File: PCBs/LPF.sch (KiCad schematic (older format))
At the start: 9 parts, among them J2 ANT

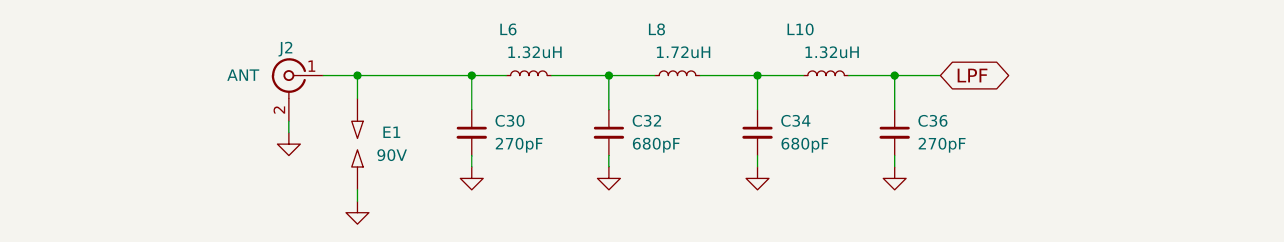
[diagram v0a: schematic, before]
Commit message: ADX988 CAT: add FE, FI commands
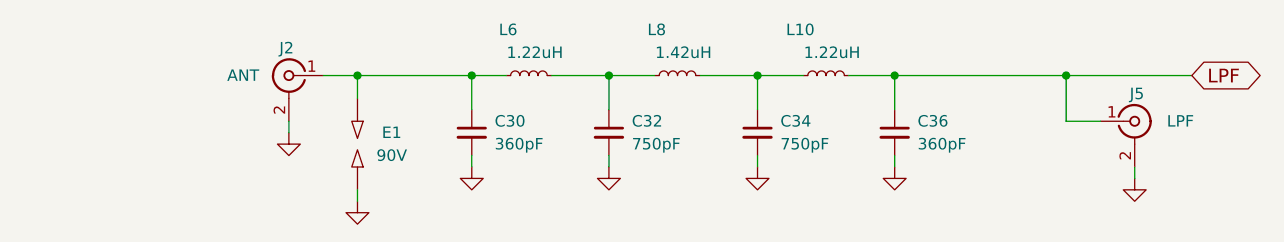
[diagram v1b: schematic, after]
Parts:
- added J5: LPF, LCSDR:U.FL_Molex_MCRF_73412-0110_Vertical, symbol Conn_Coaxial
- C30, C36: value 270pF -> 360pF; footprint Capacitors_THT:C_Disc_D4.7mm_W2.5mm_P5.00mm -> LCSDR:C_1206_0603
- C32, C34: value 680pF -> 750pF; footprint Capacitors_THT:C_Disc_D4.7mm_W2.5mm_P5.00mm -> LCSDR:C_1206_0603
- L10, L6: value 1.32uH -> 1.22uH; footprint Choke_Axial_ThroughHole:Choke_Horizontal_RM20mm -> Choke_Toroid_ThroughHole:Choke_Toroid_6,5x13mm_Vertical
- L8: value 1.72uH -> 1.42uH; footprint Choke_Axial_ThroughHole:Choke_Horizontal_RM20mm -> Choke_Toroid_ThroughHole:Choke_Toroid_6,5x13mm_Vertical
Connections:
- net GND: now also J5.2 (Ext)
- net LPF: now also J5.1 (In)
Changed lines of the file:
@@
 $Descr A4 11693 8268
 encoding utf-8
-Sheet 7 9
+Sheet 7 8
 Title ""
 Date ""
@@
 P 5200 2400
 F 0 "L6" V 5400 2450 50  0000 L CNN
-F 1 "1.32uH" V 5300 2250 50  0000 L CNN
-F 2 "Choke_Axial_ThroughHole:Choke_Horizontal_RM20mm" H 5200 2400 50  0001 C CNN
+F 1 "1.22uH" V 5300 2250 50  0000 L CNN
+F 2 "Choke_Toroid_ThroughHole:Choke_Toroid_6,5x13mm_Vertical" H 5200 2400 50  0001 C CNN
 F 3 "" H 5200 2400 50  0001 C CNN
 	1    5200 2400
@@
 P 5550 2650
 F 0 "C32" H 5650 2700 50  0000 L CNN
-F 1 "680pF" H 5650 2600 50  0000 L CNN
-F 2 "Capacitors_THT:C_Disc_D4.7mm_W2.5mm_P5.00mm" H 5550 2650 50  0001 C CNN
+F 1 "750pF" H 5650 2600 50  0000 L CNN
+F 2 "LCSDR:C_1206_0603" H 5550 2650 50  0001 C CNN
 F 3 "" H 5550 2650 50  0001 C CNN
 	1    5550 2650
@@
 P 4950 2650
 F 0 "C30" H 5050 2700 50  0000 L CNN
-F 1 "270pF" H 5050 2600 50  0000 L CNN
-F 2 "Capacitors_THT:C_Disc_D4.7mm_W2.5mm_P5.00mm" H 4950 2650 50  0001 C CNN
+F 1 "360pF" H 5050 2600 50  0000 L CNN
+F 2 "LCSDR:C_1206_0603" H 4950 2650 50  0001 C CNN
 F 3 "" H 4950 2650 50  0001 C CNN
 	1    4950 2650
@@
 P 5850 2400
 F 0 "L8" V 6050 2450 50  0000 L CNN
-F 1 "1.72uH" V 5950 2250 50  0000 L CNN
-F 2 "Choke_Axial_ThroughHole:Choke_Horizontal_RM20mm" H 5850 2400 50  0001 C CNN
+F 1 "1.42uH" V 5950 2250 50  0000 L CNN
+F 2 "Choke_Toroid_ThroughHole:Choke_Toroid_6,5x13mm_Vertical" H 5850 2400 50  0001 C CNN
 F 3 "" H 5850 2400 50  0001 C CNN
 	1    5850 2400
@@
 P 6500 2400
 F 0 "L10" V 6700 2450 50  0000 L CNN
-F 1 "1.32uH" V 6600 2250 50  0000 L CNN
-F 2 "Choke_Axial_ThroughHole:Choke_Horizontal_RM20mm" H 6500 2400 50  0001 C CNN
+F 1 "1.22uH" V 6600 2250 50  0000 L CNN
+F 2 "Choke_Toroid_ThroughHole:Choke_Toroid_6,5x13mm_Vertical" H 6500 2400 50  0001 C CNN
 F 3 "" H 6500 2400 50  0001 C CNN
 	1    6500 2400
@@
 $EndComp
 $Comp
-L GND #PWR084
+L GND #PWR92
 U 1 1 630B845A
 P 4950 2800
-F 0 "#PWR084" H 4950 2550 50  0001 C CNN
+F 0 "#PWR92" H 4950 2550 50  0001 C CNN
 F 1 "GND" H 4950 2650 50  0001 C CNN
 F 2 "" H 4950 2800 50  0001 C CNN
@@
 	4950 2800 4950 2750
 $Comp
-L GND #PWR085
+L GND #PWR93
 U 1 1 630B84B3
 P 5550 2800
-F 0 "#PWR085" H 5550 2550 50  0001 C CNN
+F 0 "#PWR93" H 5550 2550 50  0001 C CNN
 F 1 "GND" H 5550 2650 50  0001 C CNN
 F 2 "" H 5550 2800 50  0001 C CNN
@@
 	5550 2800 5550 2750
 $Comp
-L GND #PWR086
+L GND #PWR94
 U 1 1 630B84EC
 P 6200 2800
-F 0 "#PWR086" H 6200 2550 50  0001 C CNN
+F 0 "#PWR94" H 6200 2550 50  0001 C CNN
 F 1 "GND" H 6200 2650 50  0001 C CNN
 F 2 "" H 6200 2800 50  0001 C CNN
@@
 P 6200 2650
 F 0 "C34" H 6300 2700 50  0000 L CNN
-F 1 "680pF" H 6300 2600 50  0000 L CNN
-F 2 "Capacitors_THT:C_Disc_D4.7mm_W2.5mm_P5.00mm" H 6200 2650 50  0001 C CNN
+F 1 "750pF" H 6300 2600 50  0000 L CNN
+F 2 "LCSDR:C_1206_0603" H 6200 2650 50  0001 C CNN
 F 3 "" H 6200 2650 50  0001 C CNN
 	1    6200 2650
@@
 	6200 2750 6200 2800
 Wire Wire Line
-	6600 2400 7000 2400
+	6600 2400 8100 2400
 Wire Wire Line
 	6800 2400 6800 2550
 $Comp
-L GND #PWR087
+L GND #PWR95
 U 1 1 630B859B
 P 6800 2800
-F 0 "#PWR087" H 6800 2550 50  0001 C CNN
+F 0 "#PWR95" H 6800 2550 50  0001 C CNN
 F 1 "GND" H 6800 2650 50  0001 C CNN
 F 2 "" H 6800 2800 50  0001 C CNN
@@
 P 6800 2650
 F 0 "C36" H 6900 2700 50  0000 L CNN
-F 1 "270pF" H 6900 2600 50  0000 L CNN
-F 2 "Capacitors_THT:C_Disc_D4.7mm_W2.5mm_P5.00mm" H 6800 2650 50  0001 C CNN
+F 1 "360pF" H 6900 2600 50  0000 L CNN
+F 2 "LCSDR:C_1206_0603" H 6800 2650 50  0001 C CNN
 F 3 "" H 6800 2650 50  0001 C CNN
 	1    6800 2650
@@
 Connection ~ 4450 2400
 $Comp
-L GND #PWR088
+L GND #PWR91
 U 1 1 630B8EE3
 P 4450 2950
-F 0 "#PWR088" H 4450 2700 50  0001 C CNN
+F 0 "#PWR91" H 4450 2700 50  0001 C CNN
 F 1 "GND" H 4450 2800 50  0001 C CNN
 F 2 "" H 4450 2950 50  0001 C CNN
@@
 	4450 2950 4450 2900
 $Comp
-L GND #PWR089
+L GND #PWR90
 U 1 1 630B8F7F
 P 4150 2650
-F 0 "#PWR089" H 4150 2400 50  0001 C CNN
+F 0 "#PWR90" H 4150 2400 50  0001 C CNN
 F 1 "GND" H 4150 2500 50  0001 C CNN
 F 2 "" H 4150 2650 50  0001 C CNN
@@
 	4150 2650 4150 2600
 Connection ~ 6800 2400
-Text GLabel 7000 2400 2    60   BiDi ~ 0
+Text GLabel 8100 2400 2    60   BiDi ~ 0
 LPF
+$Comp
+L Conn_Coaxial J5
+U 1 1 63329C77
+P 7850 2600
+F 0 "J5" H 7860 2720 50  0000 C CNN
+F 1 "LPF" H 8050 2600 50  0000 C CNN
+F 2 "LCSDR:U.FL_Molex_MCRF_73412-0110_Vertical" H 7850 2600 50  0001 C CNN
+F 3 "" H 7850 2600 50  0001 C CNN
+	1    7850 2600
+	1    0    0    -1
+$EndComp
+Wire Wire Line
+	7700 2600 7550 2600
+Wire Wire Line
+	7550 2600 7550 2400
+Connection ~ 7550 2400
+$Comp
+L GND #PWR96
+U 1 1 63329DD2
+P 7850 2850
+F 0 "#PWR96" H 7850 2600 50  0001 C CNN
+F 1 "GND" H 7850 2700 50  0001 C CNN
+F 2 "" H 7850 2850 50  0001 C CNN
+F 3 "" H 7850 2850 50  0001 C CNN
+	1    7850 2850
+	1    0    0    -1
+$EndComp
+Wire Wire Line
+	7850 2850 7850 2800
 $EndSCHEMATC

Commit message: discret, simple, CH340E
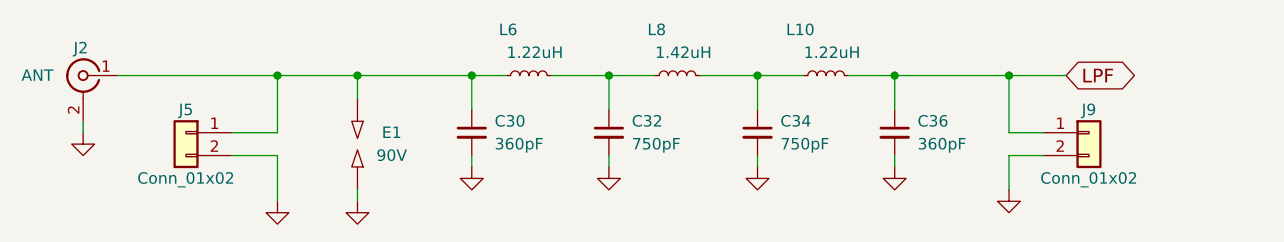
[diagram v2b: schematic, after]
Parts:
- removed J5: LPF, LCSDR:U.FL_Molex_MCRF_73412-0110_Vertical, symbol Conn_Coaxial
- added J5, J9: Conn_01x02, Pin_Headers:Pin_Header_Straight_1x02_Pitch2.54mm, symbol Conn_01x02
- L10, L6, L8: footprint Choke_Toroid_ThroughHole:Choke_Toroid_6,5x13mm_Vertical -> Choke_Toroid_ThroughHole:Choke_Toroid_5x10mm_Vertical
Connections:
- net GND: now also J5.2 (Pin_2), J9.2 (Pin_2)
- net LPF: now also J9.1 (Pin_1)
- net at C30.1, E1.1, J2.1 (In)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: now also J5.1 (Pin_1)
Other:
- moved on the sheet: J2
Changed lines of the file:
@@
 LIBS:BF998
 LIBS:relays
+LIBS:stm32
+LIBS:Interface_USB
+LIBS:Arduino
 LIBS:LCSDR-cache
 EELAYER 25 0
@@
 F 0 "L6" V 5400 2450 50  0000 L CNN
 F 1 "1.22uH" V 5300 2250 50  0000 L CNN
-F 2 "Choke_Toroid_ThroughHole:Choke_Toroid_6,5x13mm_Vertical" H 5200 2400 50  0001 C CNN
+F 2 "Choke_Toroid_ThroughHole:Choke_Toroid_5x10mm_Vertical" H 5200 2400 50  0001 C CNN
 F 3 "" H 5200 2400 50  0001 C CNN
 	1    5200 2400
@@
 	4950 2400 4950 2550
 Wire Wire Line
-	4300 2400 5100 2400
+	3400 2400 5100 2400
 $Comp
 L L_Small L8
@@
 F 0 "L8" V 6050 2450 50  0000 L CNN
 F 1 "1.42uH" V 5950 2250 50  0000 L CNN
-F 2 "Choke_Toroid_ThroughHole:Choke_Toroid_6,5x13mm_Vertical" H 5850 2400 50  0001 C CNN
+F 2 "Choke_Toroid_ThroughHole:Choke_Toroid_5x10mm_Vertical" H 5850 2400 50  0001 C CNN
 F 3 "" H 5850 2400 50  0001 C CNN
 	1    5850 2400
@@
 F 0 "L10" V 6700 2450 50  0000 L CNN
 F 1 "1.22uH" V 6600 2250 50  0000 L CNN
-F 2 "Choke_Toroid_ThroughHole:Choke_Toroid_6,5x13mm_Vertical" H 6500 2400 50  0001 C CNN
+F 2 "Choke_Toroid_ThroughHole:Choke_Toroid_5x10mm_Vertical" H 6500 2400 50  0001 C CNN
 F 3 "" H 6500 2400 50  0001 C CNN
 	1    6500 2400
@@
 $EndComp
 $Comp
-L GND #PWR92
+L GND #PWR083
 U 1 1 630B845A
 P 4950 2800
-F 0 "#PWR92" H 4950 2550 50  0001 C CNN
+F 0 "#PWR083" H 4950 2550 50  0001 C CNN
 F 1 "GND" H 4950 2650 50  0001 C CNN
 F 2 "" H 4950 2800 50  0001 C CNN
@@
 	4950 2800 4950 2750
 $Comp
-L GND #PWR93
+L GND #PWR084
 U 1 1 630B84B3
 P 5550 2800
-F 0 "#PWR93" H 5550 2550 50  0001 C CNN
+F 0 "#PWR084" H 5550 2550 50  0001 C CNN
 F 1 "GND" H 5550 2650 50  0001 C CNN
 F 2 "" H 5550 2800 50  0001 C CNN
@@
 	5550 2800 5550 2750
 $Comp
-L GND #PWR94
+L GND #PWR085
 U 1 1 630B84EC
 P 6200 2800
-F 0 "#PWR94" H 6200 2550 50  0001 C CNN
+F 0 "#PWR085" H 6200 2550 50  0001 C CNN
 F 1 "GND" H 6200 2650 50  0001 C CNN
 F 2 "" H 6200 2800 50  0001 C CNN
@@
 	6200 2750 6200 2800
 Wire Wire Line
-	6600 2400 8100 2400
+	6600 2400 7550 2400
 Wire Wire Line
 	6800 2400 6800 2550
 $Comp
-L GND #PWR95
+L GND #PWR086
 U 1 1 630B859B
 P 6800 2800
-F 0 "#PWR95" H 6800 2550 50  0001 C CNN
+F 0 "#PWR086" H 6800 2550 50  0001 C CNN
 F 1 "GND" H 6800 2650 50  0001 C CNN
 F 2 "" H 6800 2800 50  0001 C CNN
@@
 L Conn_Coaxial J2
 U 1 1 630B89B9
-P 4150 2400
-F 0 "J2" H 4160 2520 50  0000 C CNN
-F 1 "ANT" H 4350 2400 50  0000 C CNN
-F 2 "Connectors:SMA_THT_Jack_Straight" H 4150 2400 50  0001 C CNN
-F 3 "" H 4150 2400 50  0001 C CNN
-	1    4150 2400
+P 3250 2400
+F 0 "J2" H 3260 2520 50  0000 C CNN
+F 1 "ANT" H 3450 2400 50  0000 C CNN
+F 2 "Connectors:SMA_THT_Jack_Straight" H 3250 2400 50  0001 C CNN
+F 3 "" H 3250 2400 50  0001 C CNN
+	1    3250 2400
 	-1   0    0    -1
 $EndComp
@@
 Connection ~ 4450 2400
 $Comp
-L GND #PWR91
+L GND #PWR087
 U 1 1 630B8EE3
 P 4450 2950
-F 0 "#PWR91" H 4450 2700 50  0001 C CNN
+F 0 "#PWR087" H 4450 2700 50  0001 C CNN
 F 1 "GND" H 4450 2800 50  0001 C CNN
 F 2 "" H 4450 2950 50  0001 C CNN
@@
 	4450 2950 4450 2900
 $Comp
-L GND #PWR90
+L GND #PWR088
 U 1 1 630B8F7F
-P 4150 2650
-F 0 "#PWR90" H 4150 2400 50  0001 C CNN
-F 1 "GND" H 4150 2500 50  0001 C CNN
-F 2 "" H 4150 2650 50  0001 C CNN
-F 3 "" H 4150 2650 50  0001 C CNN
-	1    4150 2650
-	1    0    0    -1
-$EndComp
-Wire Wire Line
-	4150 2650 4150 2600
+P 3250 2650
+F 0 "#PWR088" H 3250 2400 50  0001 C CNN
+F 1 "GND" H 3250 2500 50  0001 C CNN
+F 2 "" H 3250 2650 50  0001 C CNN
+F 3 "" H 3250 2650 50  0001 C CNN
+	1    3250 2650
+	1    0    0    -1
+$EndComp
+Wire Wire Line
+	3250 2650 3250 2600
 Connection ~ 6800 2400
-Text GLabel 8100 2400 2    60   BiDi ~ 0
+Text GLabel 7550 2400 2    60   BiDi ~ 0
 LPF
 $Comp
-L Conn_Coaxial J5
-U 1 1 63329C77
-P 7850 2600
-F 0 "J5" H 7860 2720 50  0000 C CNN
-F 1 "LPF" H 8050 2600 50  0000 C CNN
-F 2 "LCSDR:U.FL_Molex_MCRF_73412-0110_Vertical" H 7850 2600 50  0001 C CNN
-F 3 "" H 7850 2600 50  0001 C CNN
-	1    7850 2600
-	1    0    0    -1
-$EndComp
-Wire Wire Line
-	7700 2600 7550 2600
-Wire Wire Line
-	7550 2600 7550 2400
-Connection ~ 7550 2400
-$Comp
-L GND #PWR96
+L GND #PWR089
 U 1 1 63329DD2
-P 7850 2850
-F 0 "#PWR96" H 7850 2600 50  0001 C CNN
-F 1 "GND" H 7850 2700 50  0001 C CNN
-F 2 "" H 7850 2850 50  0001 C CNN
-F 3 "" H 7850 2850 50  0001 C CNN
-	1    7850 2850
-	1    0    0    -1
-$EndComp
-Wire Wire Line
-	7850 2850 7850 2800
+P 7300 2900
+F 0 "#PWR089" H 7300 2650 50  0001 C CNN
+F 1 "GND" H 7300 2750 50  0001 C CNN
+F 2 "" H 7300 2900 50  0001 C CNN
+F 3 "" H 7300 2900 50  0001 C CNN
+	1    7300 2900
+	1    0    0    -1
+$EndComp
+Wire Wire Line
+	7300 2750 7300 2900
+$Comp
+L Conn_01x02 J9
+U 1 1 6382ECD5
+P 7650 2650
+F 0 "J9" H 7650 2750 50  0000 C CNN
+F 1 "Conn_01x02" H 7650 2450 50  0000 C CNN
+F 2 "Pin_Headers:Pin_Header_Straight_1x02_Pitch2.54mm" H 7650 2650 50  0001 C CNN
+F 3 "" H 7650 2650 50  0001 C CNN
+	1    7650 2650
+	1    0    0    -1
+$EndComp
+Wire Wire Line
+	7450 2750 7300 2750
+Wire Wire Line
+	7450 2650 7300 2650
+$Comp
+L Conn_01x02 J5
+U 1 1 6382EE85
+P 3700 2650
+F 0 "J5" H 3700 2750 50  0000 C CNN
+F 1 "Conn_01x02" H 3700 2450 50  0000 C CNN
+F 2 "Pin_Headers:Pin_Header_Straight_1x02_Pitch2.54mm" H 3700 2650 50  0001 C CNN
+F 3 "" H 3700 2650 50  0001 C CNN
+	1    3700 2650
+	-1   0    0    -1
+$EndComp
+Wire Wire Line
+	3900 2650 4100 2650
+Wire Wire Line
+	4100 2650 4100 2400
+Connection ~ 4100 2400
+$Comp
+L GND #PWR090
+U 1 1 6382F110
+P 4100 2950
+F 0 "#PWR090" H 4100 2700 50  0001 C CNN
+F 1 "GND" H 4100 2800 50  0001 C CNN
+F 2 "" H 4100 2950 50  0001 C CNN
+F 3 "" H 4100 2950 50  0001 C CNN
+	1    4100 2950
+	1    0    0    -1
+$EndComp
+Wire Wire Line
+	3900 2750 4100 2750
+Wire Wire Line
+	4100 2750 4100 2950
+Wire Wire Line
+	7300 2650 7300 2400
+Connection ~ 7300 2400
 $EndSCHEMATC

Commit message: INIT project, si5351 generate properly frequency
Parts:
- C30, C32, C34, C36: footprint LCSDR:C_1206_0603 -> Capacitors_SMD:C_0603_HandSoldering
- L10, L6: value 1.22uH -> 1.42uH
- L8: value 1.42uH -> 1.62uH
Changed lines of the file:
@@
 $Descr A4 11693 8268
 encoding utf-8
-Sheet 7 8
+Sheet 7 7
 Title ""
 Date ""
@@
 P 5200 2400
 F 0 "L6" V 5400 2450 50  0000 L CNN
-F 1 "1.22uH" V 5300 2250 50  0000 L CNN
+F 1 "1.42uH" V 5300 2250 50  0000 L CNN
 F 2 "Choke_Toroid_ThroughHole:Choke_Toroid_5x10mm_Vertical" H 5200 2400 50  0001 C CNN
 F 3 "" H 5200 2400 50  0001 C CNN
@@
 F 0 "C32" H 5650 2700 50  0000 L CNN
 F 1 "750pF" H 5650 2600 50  0000 L CNN
-F 2 "LCSDR:C_1206_0603" H 5550 2650 50  0001 C CNN
+F 2 "Capacitors_SMD:C_0603_HandSoldering" H 5550 2650 50  0001 C CNN
 F 3 "" H 5550 2650 50  0001 C CNN
 	1    5550 2650
@@
 F 0 "C30" H 5050 2700 50  0000 L CNN
 F 1 "360pF" H 5050 2600 50  0000 L CNN
-F 2 "LCSDR:C_1206_0603" H 4950 2650 50  0001 C CNN
+F 2 "Capacitors_SMD:C_0603_HandSoldering" H 4950 2650 50  0001 C CNN
 F 3 "" H 4950 2650 50  0001 C CNN
 	1    4950 2650
@@
 P 5850 2400
 F 0 "L8" V 6050 2450 50  0000 L CNN
-F 1 "1.42uH" V 5950 2250 50  0000 L CNN
+F 1 "1.62uH" V 5950 2250 50  0000 L CNN
 F 2 "Choke_Toroid_ThroughHole:Choke_Toroid_5x10mm_Vertical" H 5850 2400 50  0001 C CNN
 F 3 "" H 5850 2400 50  0001 C CNN
@@
 P 6500 2400
 F 0 "L10" V 6700 2450 50  0000 L CNN
-F 1 "1.22uH" V 6600 2250 50  0000 L CNN
+F 1 "1.42uH" V 6600 2250 50  0000 L CNN
 F 2 "Choke_Toroid_ThroughHole:Choke_Toroid_5x10mm_Vertical" H 6500 2400 50  0001 C CNN
 F 3 "" H 6500 2400 50  0001 C CNN
@@
 $EndComp
 $Comp
-L GND #PWR083
+L GND #PWR079
 U 1 1 630B845A
 P 4950 2800
-F 0 "#PWR083" H 4950 2550 50  0001 C CNN
+F 0 "#PWR079" H 4950 2550 50  0001 C CNN
 F 1 "GND" H 4950 2650 50  0001 C CNN
 F 2 "" H 4950 2800 50  0001 C CNN
@@
 	4950 2800 4950 2750
 $Comp
-L GND #PWR084
+L GND #PWR080
 U 1 1 630B84B3
 P 5550 2800
-F 0 "#PWR084" H 5550 2550 50  0001 C CNN
+F 0 "#PWR080" H 5550 2550 50  0001 C CNN
 F 1 "GND" H 5550 2650 50  0001 C CNN
 F 2 "" H 5550 2800 50  0001 C CNN
@@
 	5550 2800 5550 2750
 $Comp
-L GND #PWR085
+L GND #PWR081
 U 1 1 630B84EC
 P 6200 2800
-F 0 "#PWR085" H 6200 2550 50  0001 C CNN
+F 0 "#PWR081" H 6200 2550 50  0001 C CNN
 F 1 "GND" H 6200 2650 50  0001 C CNN
 F 2 "" H 6200 2800 50  0001 C CNN
@@
 F 0 "C34" H 6300 2700 50  0000 L CNN
 F 1 "750pF" H 6300 2600 50  0000 L CNN
-F 2 "LCSDR:C_1206_0603" H 6200 2650 50  0001 C CNN
+F 2 "Capacitors_SMD:C_0603_HandSoldering" H 6200 2650 50  0001 C CNN
 F 3 "" H 6200 2650 50  0001 C CNN
 	1    6200 2650
@@
 	6800 2400 6800 2550
 $Comp
-L GND #PWR086
+L GND #PWR082
 U 1 1 630B859B
 P 6800 2800
-F 0 "#PWR086" H 6800 2550 50  0001 C CNN
+F 0 "#PWR082" H 6800 2550 50  0001 C CNN
 F 1 "GND" H 6800 2650 50  0001 C CNN
 F 2 "" H 6800 2800 50  0001 C CNN
@@
 F 0 "C36" H 6900 2700 50  0000 L CNN
 F 1 "360pF" H 6900 2600 50  0000 L CNN
-F 2 "LCSDR:C_1206_0603" H 6800 2650 50  0001 C CNN
+F 2 "Capacitors_SMD:C_0603_HandSoldering" H 6800 2650 50  0001 C CNN
 F 3 "" H 6800 2650 50  0001 C CNN
 	1    6800 2650
@@
 Connection ~ 4450 2400
 $Comp
-L GND #PWR087
+L GND #PWR083
 U 1 1 630B8EE3
 P 4450 2950
-F 0 "#PWR087" H 4450 2700 50  0001 C CNN
+F 0 "#PWR083" H 4450 2700 50  0001 C CNN
 F 1 "GND" H 4450 2800 50  0001 C CNN
 F 2 "" H 4450 2950 50  0001 C CNN
@@
 	4450 2950 4450 2900
 $Comp
-L GND #PWR088
+L GND #PWR084
 U 1 1 630B8F7F
 P 3250 2650
-F 0 "#PWR088" H 3250 2400 50  0001 C CNN
+F 0 "#PWR084" H 3250 2400 50  0001 C CNN
 F 1 "GND" H 3250 2500 50  0001 C CNN
 F 2 "" H 3250 2650 50  0001 C CNN
@@
 LPF
 $Comp
-L GND #PWR089
+L GND #PWR085
 U 1 1 63329DD2
 P 7300 2900
-F 0 "#PWR089" H 7300 2650 50  0001 C CNN
+F 0 "#PWR085" H 7300 2650 50  0001 C CNN
 F 1 "GND" H 7300 2750 50  0001 C CNN
 F 2 "" H 7300 2900 50  0001 C CNN
@@
 Connection ~ 4100 2400
 $Comp
-L GND #PWR090
+L GND #PWR086
 U 1 1 6382F110
 P 4100 2950
-F 0 "#PWR090" H 4100 2700 50  0001 C CNN
+F 0 "#PWR086" H 4100 2700 50  0001 C CNN
 F 1 "GND" H 4100 2800 50  0001 C CNN
 F 2 "" H 4100 2950 50  0001 C CNN
